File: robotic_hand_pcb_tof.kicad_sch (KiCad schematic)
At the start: 1 part, among them J13 VL53L4CD

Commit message: Update for WIP changes
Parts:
- removed J13: VL53L4CD, symbol Connector:Conn_01x03_Pin
- added J5: Conn_01x04_Pin, symbol Connector:Conn_01x04_Pin
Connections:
- net I2C_SCL: now also J5.1 (Pin_1)
- net I2C_SDA: now also J5.2 (Pin_2)
- net TOF_INT: now also J5.3 (Pin_3)
- new net TOF_XSHUT: J5.4 (Pin_4)
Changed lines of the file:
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@@
+	(wire
+		(pts
+			(xy 38.1 43.18) (xy 63.5 43.18)
+		)
+		(stroke
+			(width 0)
+			(type default)
+		)
+	)
 	(wire
 		(pts
@@
 	(text "WIP - VL53L4CD"
 		(exclude_from_sim no)
-		(at 52.832 45.212 0)
+		(at 52.578 59.182 0)
 		(effects
 			(font
@@
 				(italic yes)
 			)
+		)
+	)
+	(hierarchical_label "TOF_XSHUT"
+		(shape input)
+		(at 38.1 43.18 180)
+		(effects
+			(font
+				(size 1.27 1.27)
+			)
+			(justify right)
 		)
 	)
@@
 	)
 	(symbol
-		(lib_id "Connector:Conn_01x03_Pin")
+		(lib_id "Connector:Conn_01x04_Pin")
 		(at 68.58 38.1 0)
 		(mirror y)
@@
 		(dnp no)
 		(fields_autoplaced yes)
-		(property "Reference" "J13"
-			(at 69.85 36.8299 0)
+		(property "Reference" "J5"
+			(at 69.85 38.0999 0)
 			(effects
 				(font
@@
 			)
 		)
-		(property "Value" "VL53L4CD"
-			(at 69.85 39.3699 0)
+		(property "Value" "Conn_01x04_Pin"
+			(at 69.85 40.6399 0)
 			(effects
 				(font
@@
 			)
 		)
-		(property "Description" "Generic connector, single row, 01x03, script generated"
+		(property "Description" "Generic connector, single row, 01x04, script generated"
 			(at 68.58 38.1 0)
 			(effects
@@
 		(pin "1"
 		)
-		(pin "3"
+		(pin "4"
 		)
 		(pin "2"
 		)
+		(pin "3"
+		)
 		(instances
-			(project "robotic_hand_pcb"
+			(project ""
 				(path "/96df9010-a1f8-4419-aac0-9388de87cb21/d34df37d-94b6-45ab-99ed-47ba0f34ea70"
-					(reference "J13")
+					(reference "J5")
 					(unit 1)
 				)

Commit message: Add WIP schematic changes
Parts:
- removed J5: Conn_01x04_Pin, symbol Connector:Conn_01x04_Pin
- added U5: VL53L4CD, time_of_flight:vl53l4cd_lga12, symbol time_of_flight:vl53l4cd
- added U6: ~, adafruit:adafruit_5396_vl53l4cd, symbol adafruit:adafruit_5396_vl53l4cd
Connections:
- net TOF_INT: now also U5.7 (GPIO1), U6.7 (GPIO)
- net TOF_XSHUT: now also U5.5 (XSHUT), U6.8 (XSHUT)
- new net +3V3: U5.1 (AVDDVCSEL), U5.11 (AVDD), U5.2 (AVSSVCSEL), U6.1 (VIN)
- new net GND: U5.12 (GND), U5.3 (GND), U5.4 (GND), U5.6 (GND), U6.2 (GND)
- new net TOF_SCL: U5.10 (SCL), U6.3 (SCL)
- new net TOF_SDA: U5.9 (SDA), U6.4 (SDA)
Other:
- note added: "VL53L4CD Time of Flight Sensor"
- note removed: "WIP - VL53L4CD"

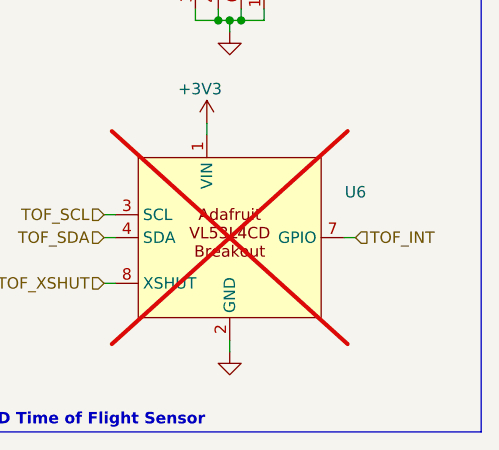
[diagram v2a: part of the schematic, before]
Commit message: Pass ERC, update component_library
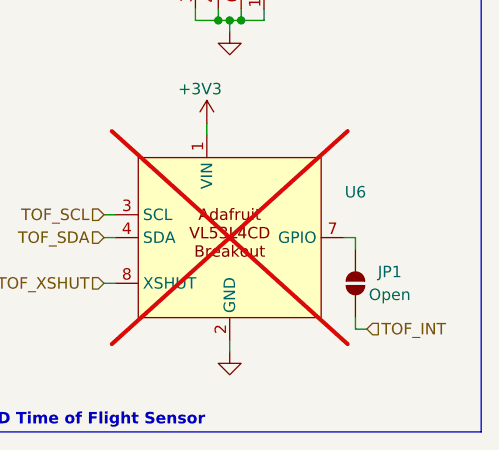
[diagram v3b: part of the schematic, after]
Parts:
- added JP1: Open, Jumper:SolderJumper-2_P1.3mm_Open_TrianglePad1.0x1.5mm, symbol Jumper:SolderJumper_2_Open
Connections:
- net TOF_INT: now also JP1.1 (A); no longer U6.7 (GPIO)
- new net: JP1.2 (B), U6.7 (GPIO)
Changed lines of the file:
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@@
+	(wire
+		(pts
+			(xy 62.23 83.82) (xy 63.5 83.82)
+		)
+		(stroke
+			(width 0)
+			(type default)
+		)
+	)
 	(wire
 		(pts
@@
 	(wire
 		(pts
+			(xy 62.23 73.66) (xy 62.23 74.93)
+		)
+		(stroke
+			(width 0)
+			(type default)
+		)
+	)
+	(wire
+		(pts
 			(xy 52.07 49.53) (xy 49.53 49.53)
+		)
+		(stroke
+			(width 0)
+			(type default)
+		)
+	)
+	(wire
+		(pts
+			(xy 62.23 82.55) (xy 62.23 83.82)
 		)
 		(stroke
@@
 		)
 	)
+	(hierarchical_label "TOF_INT"
+		(shape input)
+		(at 63.5 83.82 0)
+		(effects
+			(font
+				(size 1.27 1.27)
+			)
+			(justify left)
+		)
+	)
 	(hierarchical_label "TOF_XSHUT"
 		(shape input)
@@
 		)
 	)
+	(hierarchical_label "TOF_XSHUT"
+		(shape input)
+		(at 34.29 39.37 180)
+		(effects
+			(font
+				(size 1.27 1.27)
+			)
+			(justify right)
+		)
+	)
+	(hierarchical_label "TOF_SCL"
+		(shape input)
+		(at 34.29 71.12 180)
+		(effects
+			(font
+				(size 1.27 1.27)
+			)
+			(justify right)
+		)
+	)
+	(hierarchical_label "TOF_SCL"
+		(shape input)
+		(at 34.29 34.29 180)
+		(effects
+			(font
+				(size 1.27 1.27)
+			)
+			(justify right)
+		)
+	)
+	(hierarchical_label "TOF_SDA"
+		(shape input)
+		(at 34.29 31.75 180)
+		(effects
+			(font
+				(size 1.27 1.27)
+			)
+			(justify right)
+		)
+	)
 	(hierarchical_label "TOF_INT"
 		(shape input)
-		(at 62.23 73.66 0)
+		(at 62.23 35.56 0)
 		(effects
 			(font
@@
 		)
 	)
-	(hierarchical_label "TOF_XSHUT"
-		(shape input)
-		(at 34.29 39.37 180)
-		(effects
-			(font
-				(size 1.27 1.27)
-			)
-			(justify right)
-		)
-	)
-	(hierarchical_label "TOF_SCL"
-		(shape input)
-		(at 34.29 71.12 180)
-		(effects
-			(font
-				(size 1.27 1.27)
-			)
-			(justify right)
-		)
-	)
-	(hierarchical_label "TOF_SCL"
-		(shape input)
-		(at 34.29 34.29 180)
-		(effects
-			(font
-				(size 1.27 1.27)
-			)
-			(justify right)
-		)
-	)
-	(hierarchical_label "TOF_SDA"
-		(shape input)
-		(at 34.29 31.75 180)
-		(effects
-			(font
-				(size 1.27 1.27)
-			)
-			(justify right)
-		)
-	)
-	(hierarchical_label "TOF_INT"
-		(shape input)
-		(at 62.23 35.56 0)
-		(effects
-			(font
-				(size 1.27 1.27)
-			)
-			(justify left)
-		)
-	)
+	(symbol
+		(lib_id "Jumper:SolderJumper_2_Open")
+		(at 62.23 78.74 90)
+		(unit 1)
+		(exclude_from_sim yes)
+		(in_bom no)
+		(on_board yes)
+		(dnp no)
+		(property "Reference" "JP1"
+			(at 66.04 77.47 90)
+			(effects
+				(font
+					(size 1.27 1.27)
+				)
+			)
+		)
+		(property "Value" "Open"
+			(at 66.04 80.01 90)
+			(effects
+				(font
+					(size 1.27 1.27)
+				)
+			)
+		)
+		(property "Footprint" "Jumper:SolderJumper-2_P1.3mm_Open_TrianglePad1.0x1.5mm"
+			(at 62.23 78.74 0)
+			(effects
+				(font
+					(size 1.27 1.27)
+				)
+				(hide yes)
+			)
+		)
+		(property "Datasheet" "~"
+			(at 62.23 78.74 0)
+			(effects
+				(font
+					(size 1.27 1.27)
+				)
+				(hide yes)
+			)
+		)
+		(property "Description" "Solder Jumper, 2-pole, open"
+			(at 62.23 78.74 0)
+			(effects
+				(font
+					(size 1.27 1.27)
+				)
+				(hide yes)
+			)
+		)
+		(pin "1"
+		)
+		(pin "2"
+		)
+		(instances
+			(project "robotic_hand_pcb"
+				(path "/96df9010-a1f8-4419-aac0-9388de87cb21/d34df37d-94b6-45ab-99ed-47ba0f34ea70"
+					(reference "JP1")
+					(unit 1)
+				)
+			)
+		)
+	)

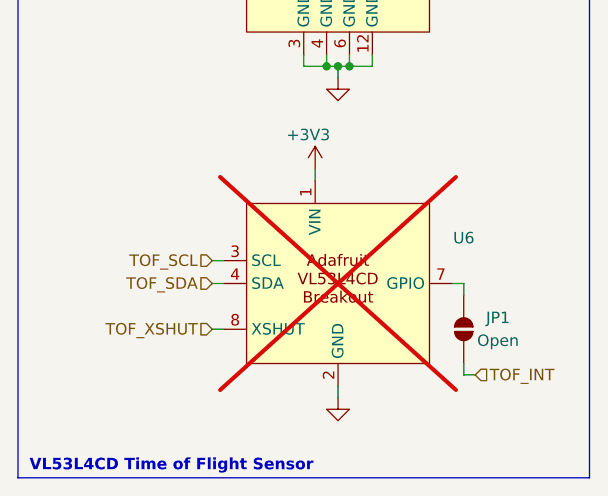
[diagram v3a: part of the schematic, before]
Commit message: Fix symbol error, update component_library
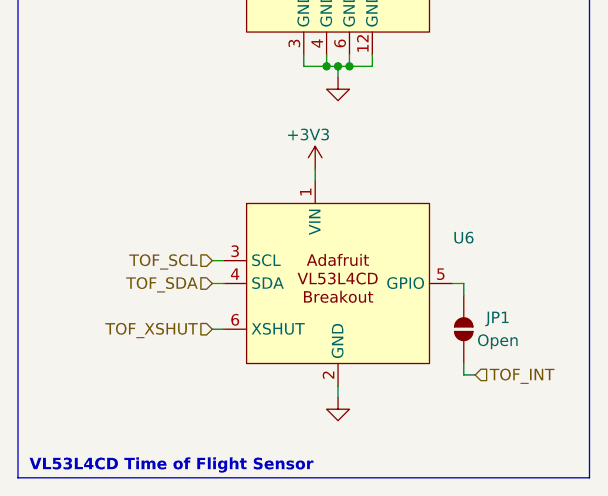
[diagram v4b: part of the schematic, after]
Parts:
- U6: now fitted
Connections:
- net TOF_XSHUT: now also U6.6 (XSHUT); no longer U6.8 (XSHUT)
- net at JP1.2 (B): now also U6.5 (GPIO); no longer U6.7 (GPIO)
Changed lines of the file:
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@@
 		(at 48.26 73.66 0)
 		(unit 1)
-		(exclude_from_sim yes)
+		(exclude_from_sim no)
 		(in_bom yes)
 		(on_board yes)
-		(dnp yes)
+		(dnp no)
 		(fields_autoplaced yes)
 		(property "Reference" "U6"
@@
 		(pin "2"
 		)
-		(pin "7"
+		(pin "5"
 		)
 		(pin "3"
@@
 		(pin "4"
 		)
-		(pin "8"
+		(pin "6"
 		)
 		(pin "1"

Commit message: Cleanup and remove unneeded connectors
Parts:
- U6: now not fitted
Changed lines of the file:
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@@
 		(in_bom yes)
 		(on_board yes)
-		(dnp no)
+		(dnp yes)
 		(fields_autoplaced yes)
 		(property "Reference" "U6"

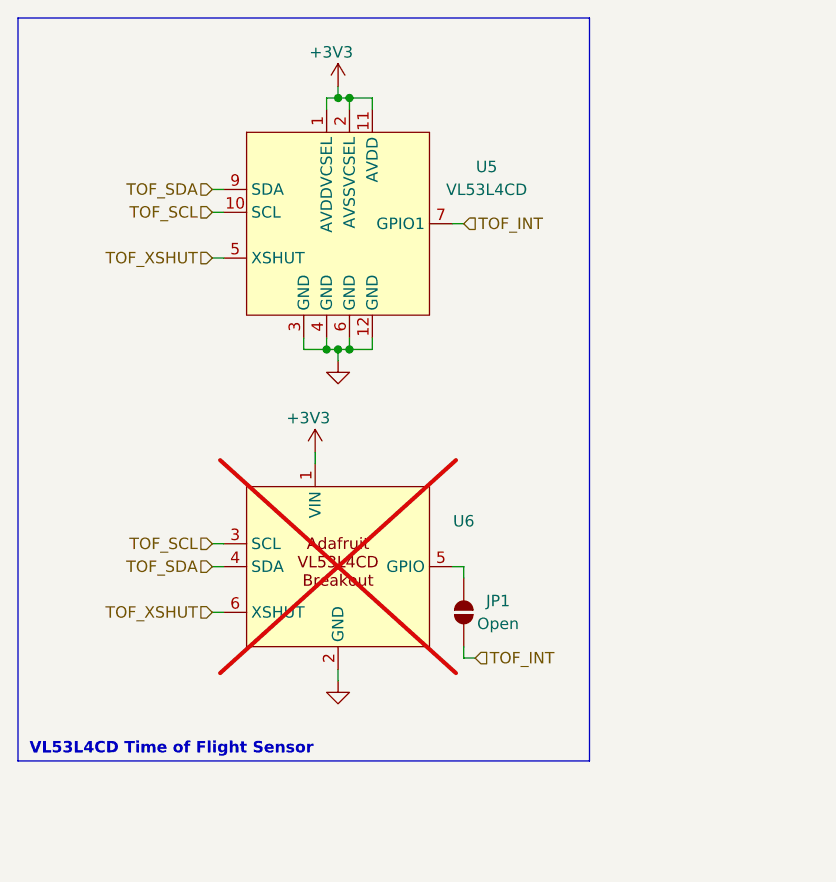
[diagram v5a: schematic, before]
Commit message: Add WIP PCB layout and routing
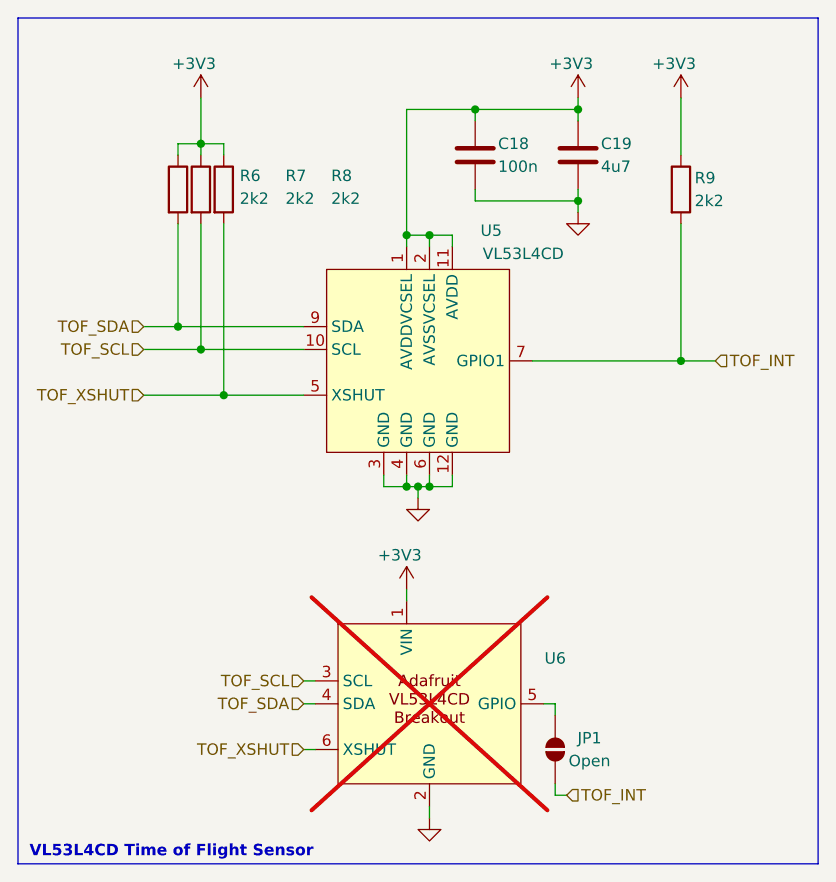
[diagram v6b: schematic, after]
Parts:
- added C18: 100n, Capacitor_SMD:C_0603_1608Metric, symbol Device:C
- added C19: 4u7, Capacitor_SMD:C_0603_1608Metric, symbol Device:C
- added R6, R7, R8, R9: 2k2, Resistor_SMD:R_0603_1608Metric, symbol Device:R
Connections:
- net +3V3: now also C18.1, C19.1, R6.1, R7.1, R8.1, R9.1
- net GND: now also C18.2, C19.2
- net TOF_INT: now also R9.2
- net TOF_SCL: now also R7.2
- net TOF_SDA: now also R6.2
- net TOF_XSHUT: now also R8.2
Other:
- moved on the sheet: JP1, U5, U6

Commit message: Swap adafruit breakout for pin header footprint
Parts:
- U6: footprint adafruit:adafruit_5396_vl53l4cd -> Connector_PinHeader_2.54mm:PinHeader_1x06_P2.54mm_Vertical; now fitted
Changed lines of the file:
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@@
 		(in_bom yes)
 		(on_board yes)
-		(dnp yes)
-		(fields_autoplaced yes)
+		(dnp no)
 		(property "Reference" "U6"
-			(at 72.39 83.8514 0)
+			(at 67.31 78.74 0)
 			(effects
 				(font
@@
 			)
 		)
-		(property "Footprint" "adafruit:adafruit_5396_vl53l4cd"
+		(property "Footprint" "Connector_PinHeader_2.54mm:PinHeader_1x06_P2.54mm_Vertical"
 			(at 58.42 88.9 0)
 			(effects
